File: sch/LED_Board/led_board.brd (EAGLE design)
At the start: 63.2 x 12.7 mm, 6 parts

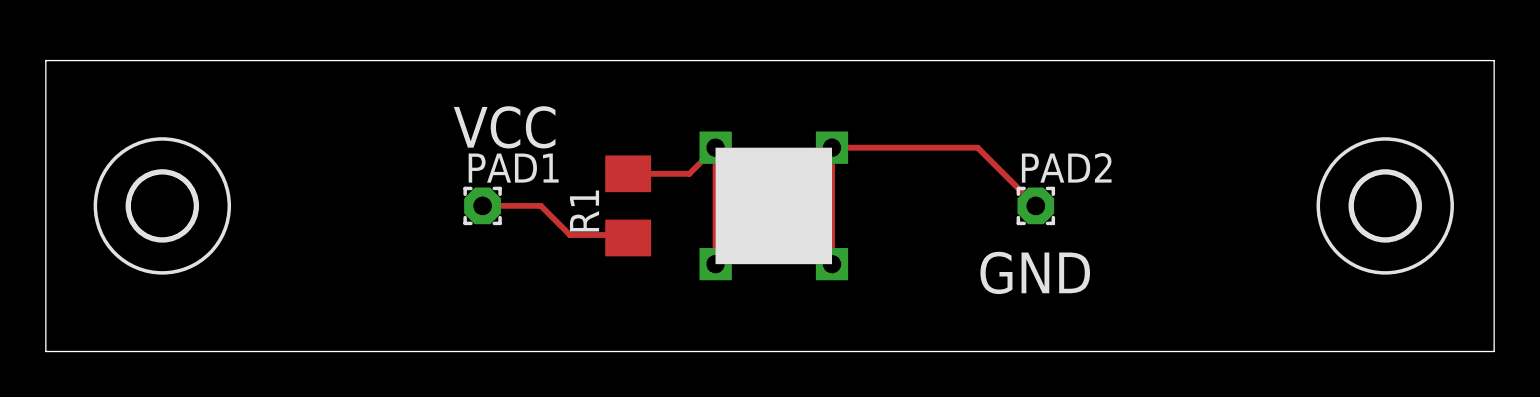
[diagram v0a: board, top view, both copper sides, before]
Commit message: More work on schematics.  Using EAGLE exclusively for now... Changed LED board to allow for an attiny4/5/9/10 with a signal pin and to use an RGB led.
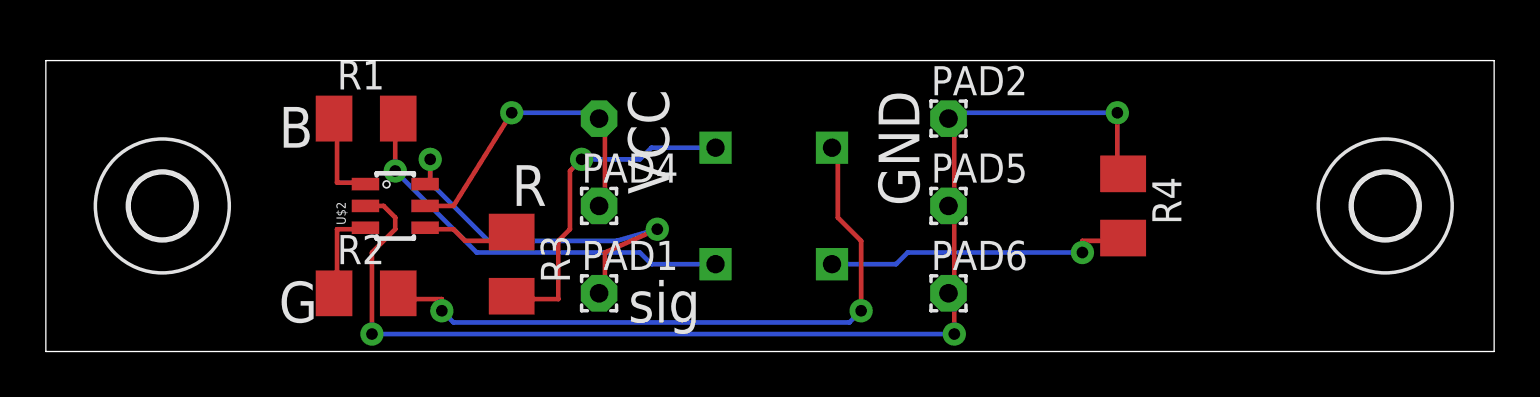
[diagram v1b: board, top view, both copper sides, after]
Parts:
- added PAD3, PAD4, PAD5, PAD6: (no value), wirepad:1,6/0,8
- added R2, R3, R4: (no value), resistor:M1206
- added U$2: ATTINY10SOT, *Personal Library:SOT23-6
- U$1: value 7.6X7.6_LED -> BIVAR-RGB-LED; device MyLib:7.6X7.6MM_LED -> *Personal Library:7.6X7.6MM-LED
- moved R1 12.0 mm to (14.0, 8.89), turned to 0 degrees
- moved PAD1 6.35 mm to (24.1, 1.27)
- moved PAD2 5.39 mm to (39.4, 8.89)
- flipped U$1 to the bottom
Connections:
- removed net GND: PAD2.1, U$1.GND1, U$1.GND2
- new net N$2: PAD2.1, PAD5.1, PAD6.1, R4.1, U$2.2
- new net N$3: R2.1, U$2.3
- new net N$4: R3.1, U$2.4
- new net N$5: R1.2, U$1.BLUE
- new net N$6: R2.2, U$1.GREEN
- new net N$7: R3.2, U$1.RED
- new net N$8: R4.2, U$1.GND
- new net N$9: PAD1.1, U$2.6
- net N$1: now also R1.1, U$2.1; no longer R1.2, U$1.VCC1, U$1.VCC2
- net VCC: now also PAD3.1, PAD4.1, U$2.5; no longer PAD1.1, R1.1
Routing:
- net N$2: track 0.00 -> 52.7 mm, vias 0 -> 3
- net N$6: track 0.00 -> 29.0 mm, vias 0 -> 2
- net N$5: track 0.00 -> 18.0 mm, vias 0 -> 1
- net N$9: track 0.00 -> 17.7 mm, vias 0 -> 2
- net GND: track 15.0 -> 0.00 mm
- net N$7: track 0.00 -> 14.7 mm, vias 0 -> 1
- net N$8: track 0.00 -> 13.4 mm, vias 0 -> 1
- net VCC: track 6.93 -> 14.1 mm, vias 0 -> 1
- net N$1: track 9.36 -> 4.07 mm
- net N$4: track 0.00 -> 4.38 mm
- net N$3: track 0.00 -> 4.07 mm
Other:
- board text added: "B"
- board text added: "G"
- board text added: "R"
- board text added: "sig"

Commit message: Added breakout for PB pins on attiny10 on the LED controller.
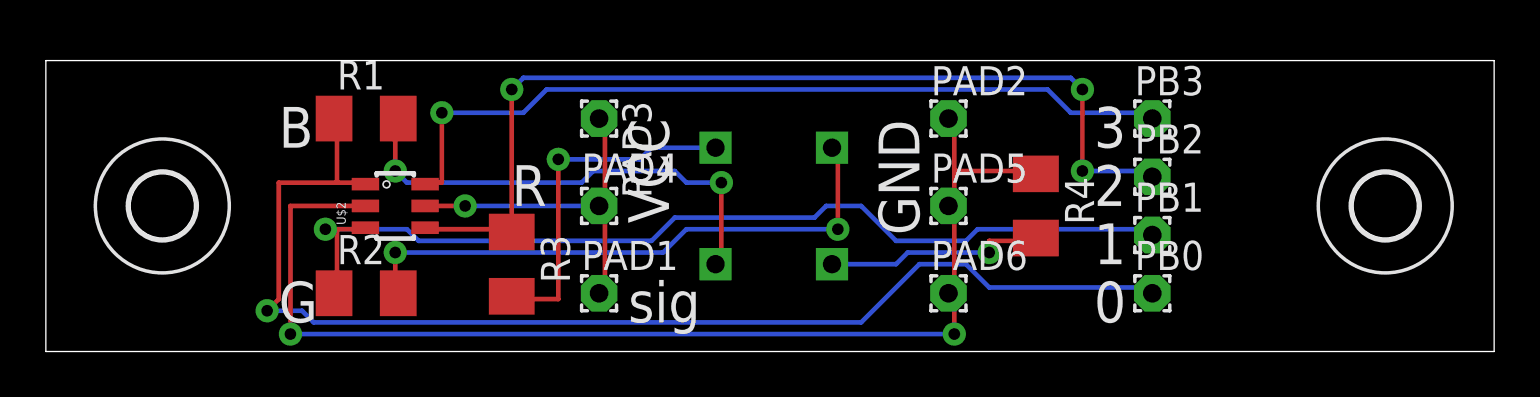
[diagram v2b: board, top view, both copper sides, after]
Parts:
- added PB0, PB1, PB2, PB3: (no value), wirepad:1,6/0,8
- moved R4 3.81 mm to (43.2, 5.08)
- flipped PAD3 to the top, turned to 270 degrees
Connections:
- removed net N$1: R1.1, U$2.1
- removed net N$3: R2.1, U$2.3
- removed net N$4: R3.1, U$2.4
- removed net N$9: PAD1.1, U$2.6
- new net PB0: PB0.1, R1.1, U$2.1
- new net PB1: PB1.1, R2.1, U$2.3
- new net PB2: PB2.1, R3.1, U$2.4
- new net PB3: PB3.1, U$2.6
- net VCC: now also PAD1.1
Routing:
- net PB0: track 0.00 -> 53.0 mm, vias 0 -> 1
- net PB1: track 0.00 -> 42.6 mm, vias 0 -> 1
- net PB2: track 0.00 -> 42.2 mm, vias 0 -> 3
- net PB3: track 0.00 -> 35.9 mm, vias 0 -> 1
- net N$9: track 17.7 -> 0.00 mm, vias 2 -> 0
- net N$4: track 4.38 -> 0.00 mm
- net N$1: track 4.07 -> 0.00 mm
- net N$3: track 4.07 -> 0.00 mm
- net N$8: track 13.4 -> 9.73 mm
- net N$6: track 29.0 -> 25.3 mm
- net N$5: track 18.0 -> 21.0 mm, vias 1 -> 2
- net VCC: track 14.1 -> 15.7 mm
- net N$2: track 52.7 -> 51.5 mm, vias 3 -> 2
- net N$7: track 14.7 -> 15.3 mm
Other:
- board text added: "0"
- board text added: "1"
- board text added: "2"
- board text added: "3"

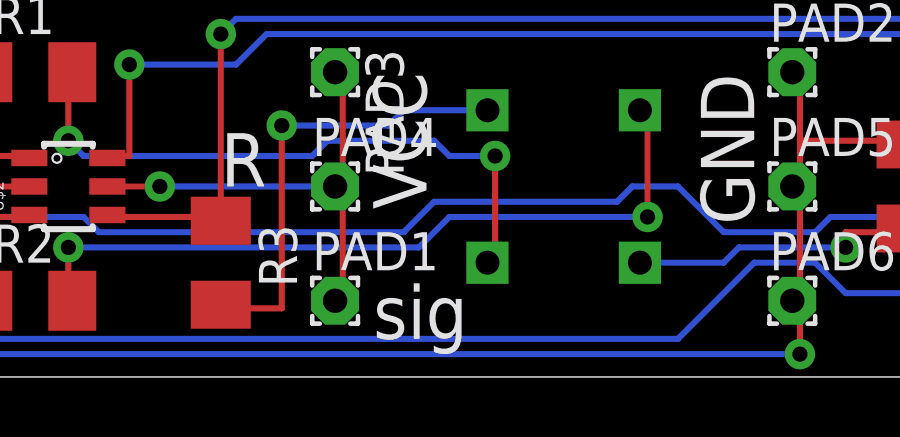
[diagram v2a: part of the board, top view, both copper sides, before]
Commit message: fixed typo in schematic, removed extra text from board
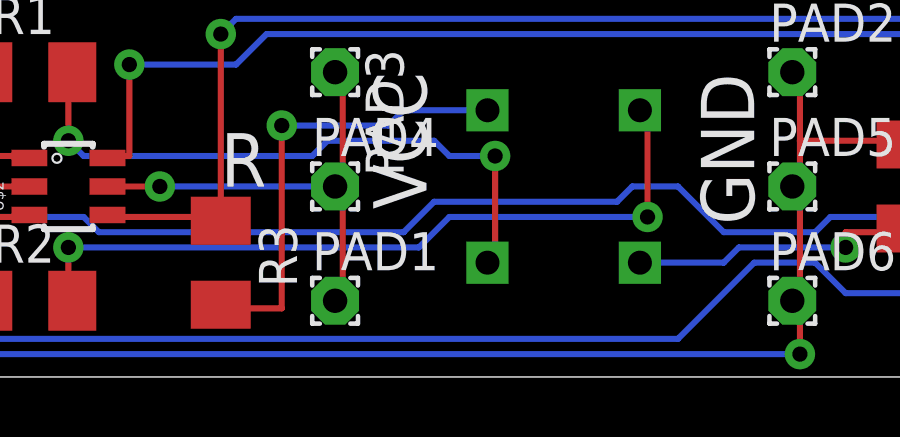
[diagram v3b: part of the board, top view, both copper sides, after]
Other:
- board text removed: "sig"
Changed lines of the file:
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@@
 <text x="10.16" y="0" size="1.778" layer="21">G</text>
 <text x="10.16" y="7.62" size="1.778" layer="21">B</text>
-<text x="25.4" y="0" size="1.778" layer="21">sig</text>
 <text x="45.72" y="0" size="1.778" layer="21">0</text>
 <text x="45.72" y="2.54" size="1.778" layer="21">1</text>
